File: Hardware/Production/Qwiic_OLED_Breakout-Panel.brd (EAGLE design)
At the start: 103 x 231.6 mm, 909 parts, among them J1 QWIIC_RIGHT_ANGLE, J10 QWIIC_RIGHT_ANGLE, J11 QWIIC_RIGHT_ANGLE, J13 QWIIC_RIGHT_ANGLE, J14 QWIIC_RIGHT_ANGLE, J16 QWIIC_RIGHT_ANGLE, J17 QWIIC_RIGHT_ANGLE, J19 QWIIC_RIGHT_ANGLE, J2 QWIIC_RIGHT_ANGLE, J20 QWIIC_RIGHT_ANGLE, J22 QWIIC_RIGHT_ANGLE, J23 QWIIC_RIGHT_ANGLE, J25 QWIIC_RIGHT_ANGLE, J26 QWIIC_RIGHT_ANGLE, J28 QWIIC_RIGHT_ANGLE, J29 QWIIC_RIGHT_ANGLE, J3 QWIIC_RIGHT_ANGLE, J31 QWIIC_RIGHT_ANGLE, J32 QWIIC_RIGHT_ANGLE, J34 QWIIC_RIGHT_ANGLE, J35 QWIIC_RIGHT_ANGLE, J37 QWIIC_RIGHT_ANGLE, J38 QWIIC_RIGHT_ANGLE, J40 QWIIC_RIGHT_ANGLE, J41 QWIIC_RIGHT_ANGLE, J43 QWIIC_RIGHT_ANGLE, J44 QWIIC_RIGHT_ANGLE, J46 QWIIC_RIGHT_ANGLE, J47 QWIIC_RIGHT_ANGLE, J49 QWIIC_RIGHT_ANGLE, J5 QWIIC_RIGHT_ANGLE, J50 QWIIC_RIGHT_ANGLE, J52 QWIIC_RIGHT_ANGLE, J53 QWIIC_RIGHT_ANGLE, J55 QWIIC_RIGHT_ANGLE, J56 QWIIC_RIGHT_ANGLE, J58 QWIIC_RIGHT_ANGLE, J59 QWIIC_RIGHT_ANGLE, J61 QWIIC_RIGHT_ANGLE, J62 QWIIC_RIGHT_ANGLE, J7 QWIIC_RIGHT_ANGLE, J8 QWIIC_RIGHT_ANGLE

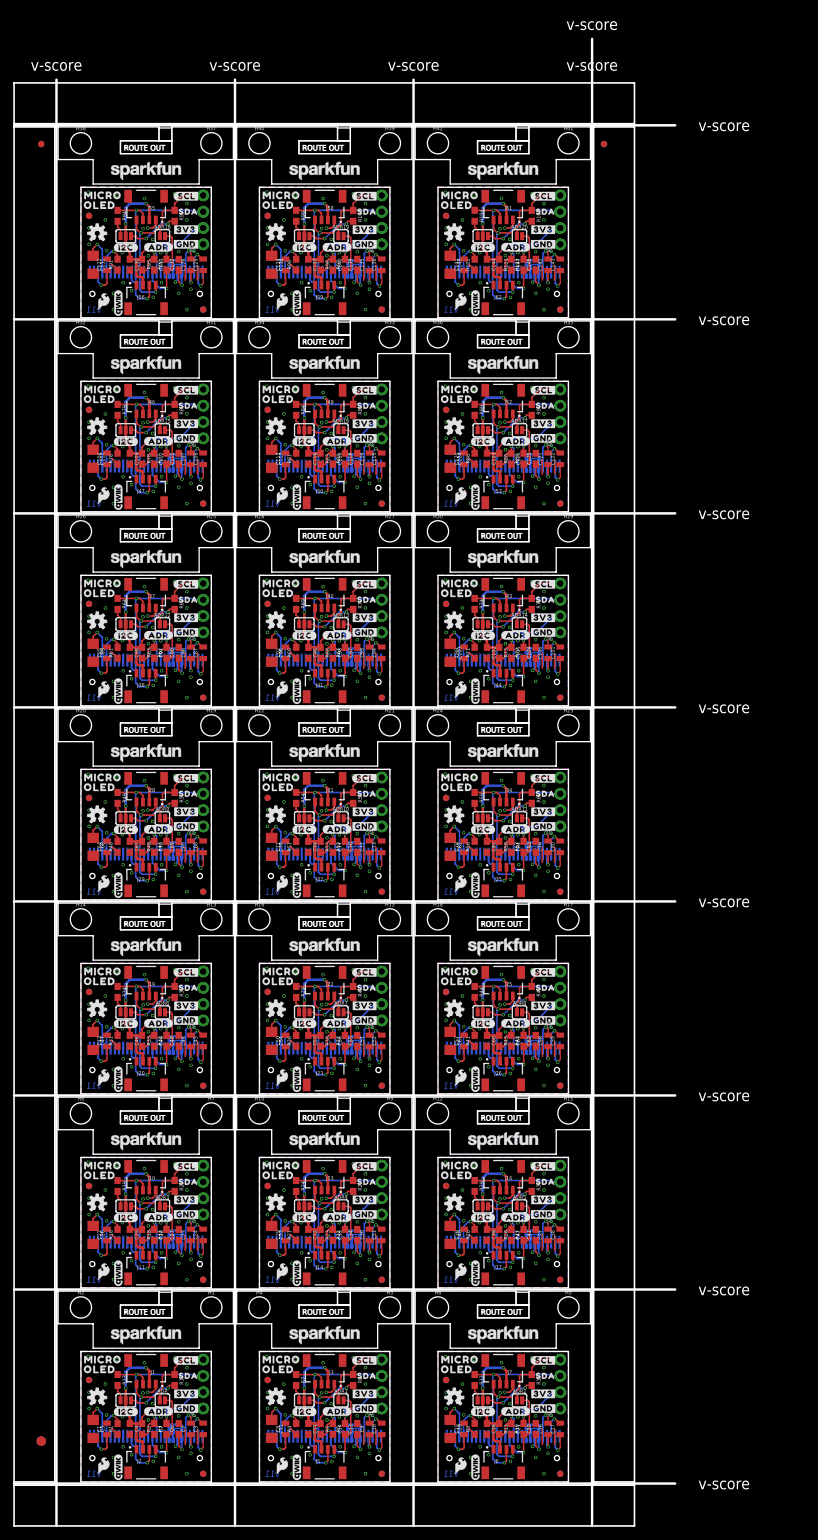
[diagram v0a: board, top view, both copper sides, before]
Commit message: Adds new panel after bringing the tabbed part to match the panel
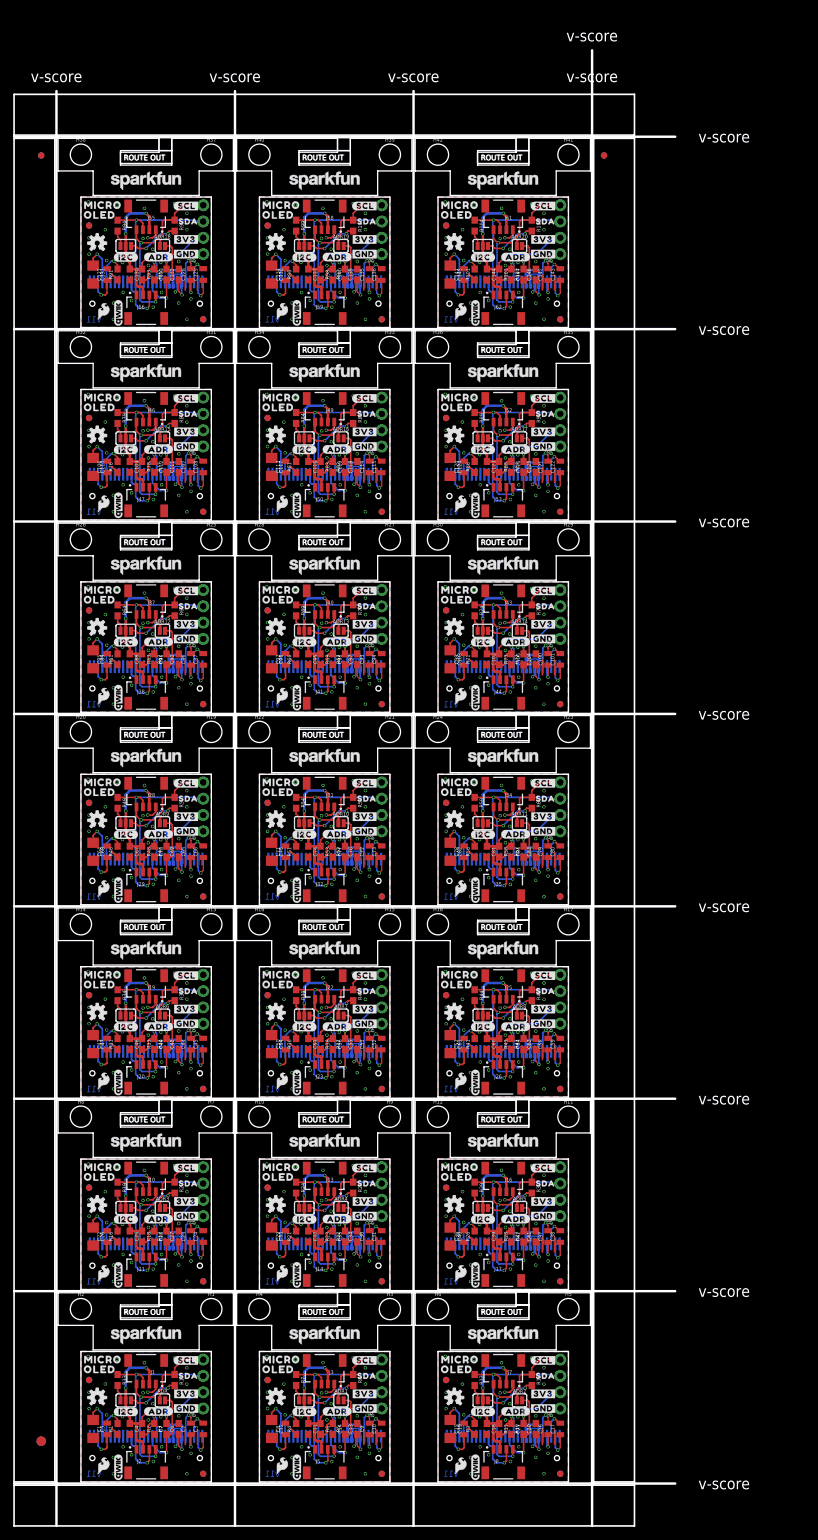
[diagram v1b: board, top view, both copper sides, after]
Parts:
- moved E$1 1.78 mm to (-2.62, 206.6)
- moved E$2 1.78 mm to (-2.62, 206.6)
- moved E$3 1.78 mm to (85.0, 206.6)
- moved E$4 1.78 mm to (85.0, 206.6)
- moved H37 1.78 mm to (23.9, 206.8)
- moved H38 1.78 mm to (3.56, 206.8)
- moved H39 1.78 mm to (51.7, 206.8)
- moved H40 1.78 mm to (31.4, 206.8)
- moved H41 1.78 mm to (79.5, 206.8)
- moved H42 1.78 mm to (59.2, 206.8)
- moved ADR18 1.52 mm to (16.3, 192.5)
- moved ADR19 1.52 mm to (44.1, 192.5)
- moved ADR20 1.52 mm to (71.9, 192.5)
- moved C127 1.52 mm to (7.62, 188.1)
- moved C128 1.52 mm to (20.7, 188.1)
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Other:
- board size 103 x 231.6 mm -> 103 x 229.9 mm

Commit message: Revised v11 panel to match v10 panel
- Adjusted rail widths, board spacing, and fiducial locations to match v10 panel
- Generated gerbers
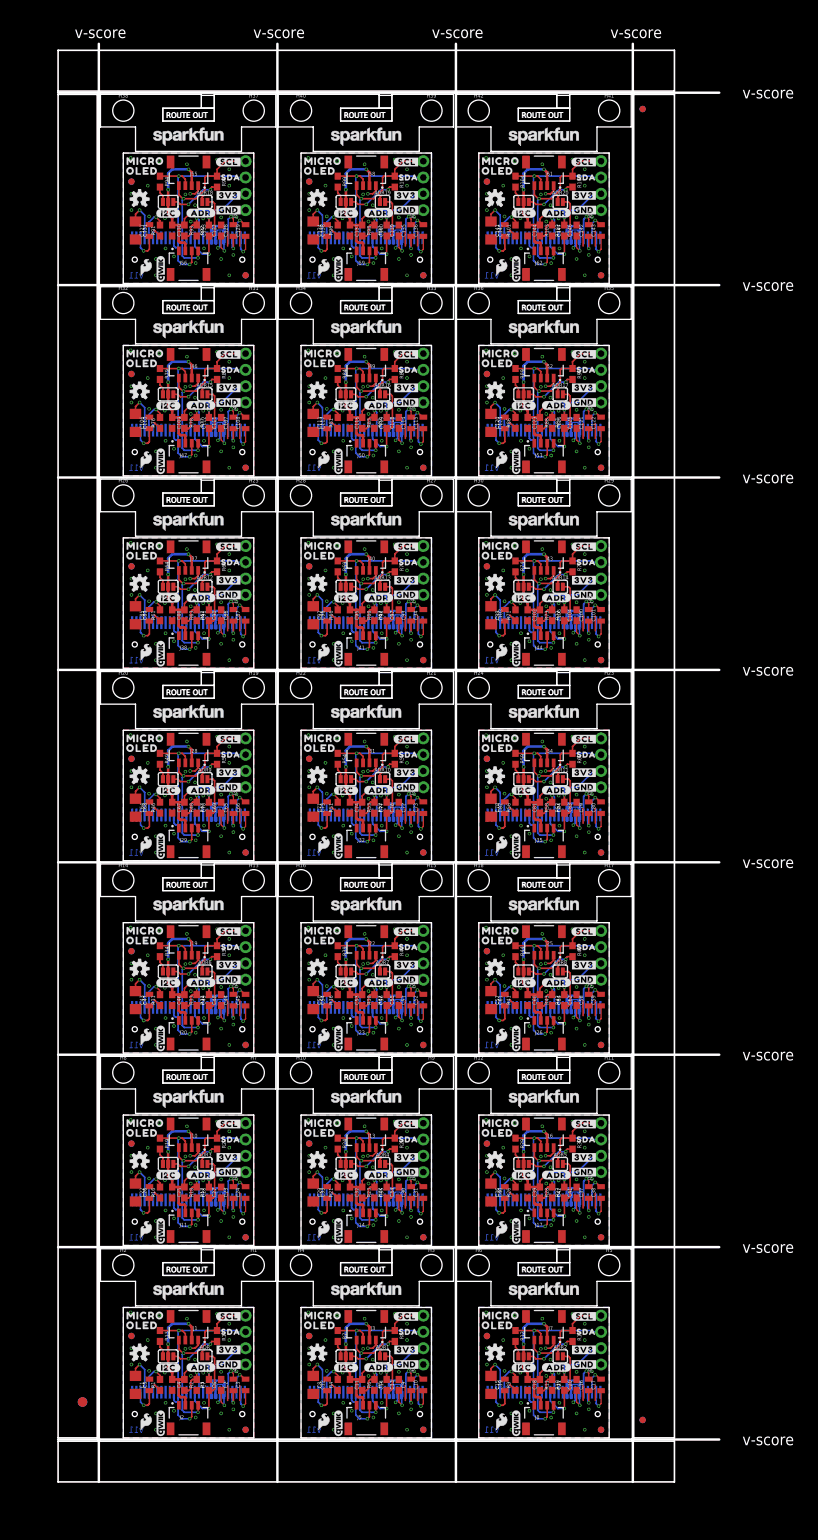
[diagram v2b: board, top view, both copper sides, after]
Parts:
- moved E$1 218.1 mm to (91.1, 9.65)
- moved E$2 218.1 mm to (91.1, 9.65)
- moved R17 9.52 mm to (23.5, 45.1)
- moved R32 9.52 mm to (23.5, 75.1)
- moved R62 9.52 mm to (23.5, 135.0)
- moved R77 9.52 mm to (23.5, 165.0)
- moved R92 9.52 mm to (23.5, 194.9)
- moved U$139 9.52 mm to (26.7, 115.7)
- moved U$144 9.52 mm to (26.7, 115.7)
- moved U$184 9.52 mm to (26.7, 145.7)
- moved U$189 9.52 mm to (26.7, 145.7)
- moved U$229 9.52 mm to (26.7, 175.6)
- moved U$234 9.52 mm to (26.7, 175.6)
- moved U$274 9.52 mm to (26.7, 205.6)
- moved U$279 9.52 mm to (26.7, 205.6)
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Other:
- board size 103 x 229.9 mm -> 103 x 224 mm
